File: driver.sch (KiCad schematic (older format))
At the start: 45 parts, among them J1 Screw_Terminal_01x02, J2 Conn_02x12_Odd_Even, Q10 Q_NMOS_GDSD, Q11 Q_NMOS_GDSD, Q12 Q_NMOS_GDSD, Q13 Q_NMOS_GDSD, Q14 Q_NMOS_GDSD, Q15 Q_NMOS_GDSD, Q16 Q_NMOS_GDSD, Q17 AOD417 Q_PMOS_DGS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

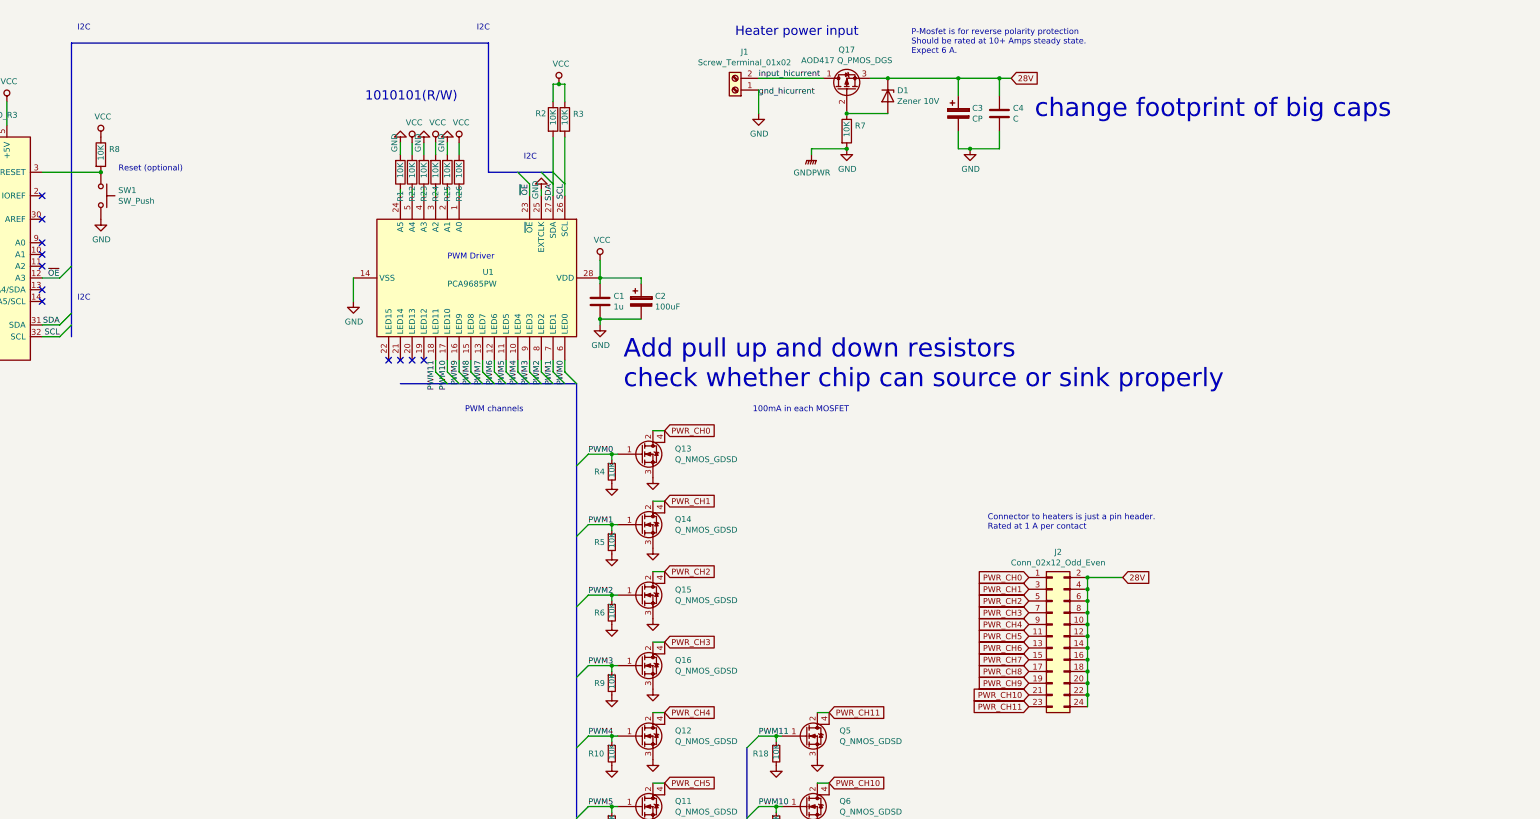
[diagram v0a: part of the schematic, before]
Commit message: remove capacitor footprints and organize.
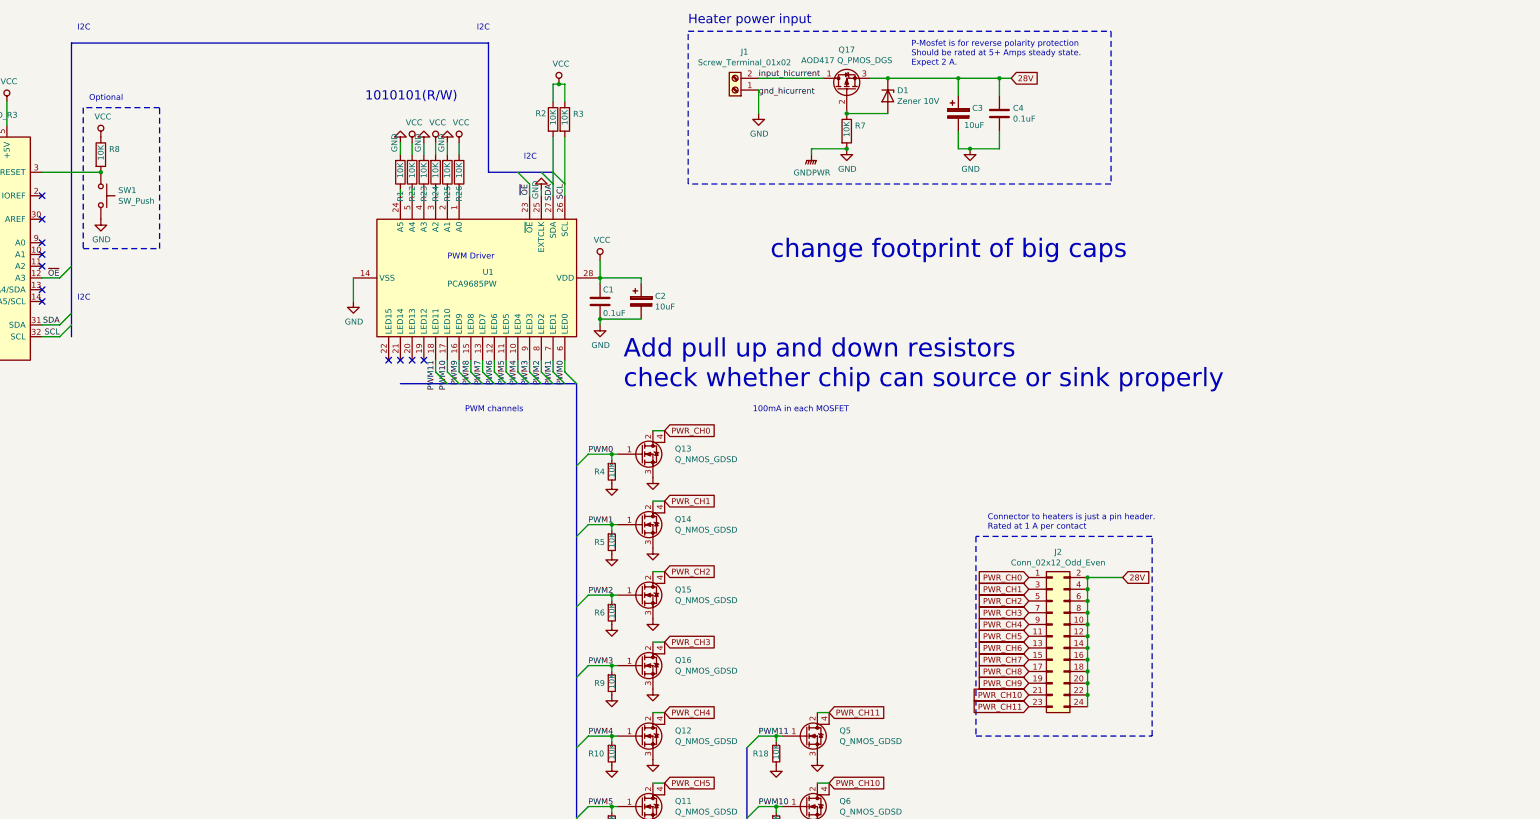
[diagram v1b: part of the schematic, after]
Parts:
- C1: value 1u -> 0.1uF; footprint Capacitor_SMD:C_0805_2012Metric_Pad1.15x1.40mm_HandSolder -> (none)
- C2: value 100uF -> 10uF; footprint Capacitor_THT:CP_Radial_D8.0mm_P3.50mm -> (none)
- C3: value CP -> 10uF
- C4: value C -> 0.1uF
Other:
- note added: "Optional"
- note added: "P-Mosfet is for reverse polarity protection\nShould be rated at 5+ Amps steady state.\nExpect 2 A."
- note removed: "P-Mosfet is for reverse polarity protection\nShould be rated at 10+ Amps steady state.\nExpect 6 A."
- note removed: "Reset (optional)"
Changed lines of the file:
@@
 U 1 1 5C1B80A4
 P 6800 3250
-F 0 "C1" H 6915 3296 50  0000 L CNN
-F 1 "1u" H 6915 3205 50  0000 L CNN
-F 2 "Capacitor_SMD:C_0805_2012Metric_Pad1.15x1.40mm_HandSolder" H 6838 3100 50  0001 C CNN
+F 0 "C1" H 6825 3350 50  0000 L CNN
+F 1 "0.1uF" H 6825 3150 50  0000 L CNN
+F 2 "" H 6838 3100 50  0001 C CNN
 F 3 "~" H 6800 3250 50  0001 C CNN
 	1    6800 3250
@@
 P 7150 3250
 F 0 "C2" H 7268 3296 50  0000 L CNN
-F 1 "100uF" H 7268 3205 50  0000 L CNN
-F 2 "Capacitor_THT:CP_Radial_D8.0mm_P3.50mm" H 7188 3100 50  0001 C CNN
+F 1 "10uF" H 7268 3205 50  0000 L CNN
+F 2 "" H 7188 3100 50  0001 C CNN
 F 3 "~" H 7150 3250 50  0001 C CNN
 	1    7150 3250
@@
 Wire Wire Line
 	8650 6750 8750 6750
-Text Notes 7950 1000 0    79   ~ 0
+Text Notes 7550 900  0    79   ~ 0
 Heater power input
 $Comp
@@
 	1    0    0    -1
 $EndComp
-Text Notes 9450 1150 0    50   ~ 0
-P-Mosfet is for reverse polarity protection\nShould be rated at 10+ Amps steady state.\nExpect 6 A.
+Text Notes 9450 1250 0    50   ~ 0
+P-Mosfet is for reverse polarity protection\nShould be rated at 5+ Amps steady state.\nExpect 2 A.
 Text GLabel 10450 5600 0    50   Input ~ 0
 PWR_CH0
@@
 Text Notes 2350 3250 0    50   ~ 0
 I2C
-Text Notes 2700 2150 0    50   ~ 0
-Reset (optional)
+Text Notes 2450 1550 0    50   ~ 0
+Optional
 Text Notes 5650 4200 0    50   ~ 0
 PWM channels
@@
 P 9850 1650
 F 0 "C3" H 9968 1696 50  0000 L CNN
-F 1 "CP" H 9968 1605 50  0000 L CNN
+F 1 "10uF" H 9900 1550 50  0000 L CNN
 F 2 "" H 9888 1500 50  0001 C CNN
 F 3 "~" H 9850 1650 50  0001 C CNN
@@
 P 10200 1650
 F 0 "C4" H 10315 1696 50  0000 L CNN
-F 1 "C" H 10315 1605 50  0000 L CNN
+F 1 "0.1uF" H 10315 1605 50  0000 L CNN
 F 2 "" H 10238 1500 50  0001 C CNN
 F 3 "~" H 10200 1650 50  0001 C CNN
@@
 Text Notes 7000 4000 0    157  ~ 0
 Add pull up and down resistors\ncheck whether chip can source or sink properly
-Text Notes 10500 1700 0    157  ~ 0
+Text Notes 8250 2900 0    157  ~ 0
 change footprint of big caps
 $Comp
@@
 Wire Wire Line
 	6500 1850 6500 2350
+Wire Notes Line
+	2400 1600 2400 2800
+Wire Notes Line
+	2400 2800 3050 2800
+Wire Notes Line
+	3050 2800 3050 1600
+Wire Notes Line
+	3050 1600 2400 1600
+Wire Notes Line
+	7550 950  11150 950
+Wire Notes Line
+	11150 950  11150 2250
+Wire Notes Line
+	11150 2250 7550 2250
+Wire Notes Line
+	7550 2250 7550 950
+Wire Notes Line
+	10000 5250 10000 6950
+Wire Notes Line
+	10000 6950 11500 6950
+Wire Notes Line
+	11500 6950 11500 5250
+Wire Notes Line
+	11500 5250 10000 5250
+Wire Wire Line
+	6400 1850 6400 2350
 Wire Bus Line
 	5850 2150 6400 2150
-Wire Wire Line
-	6400 1850 6400 2350
 Wire Bus Line
 	8050 7050 8050 9400

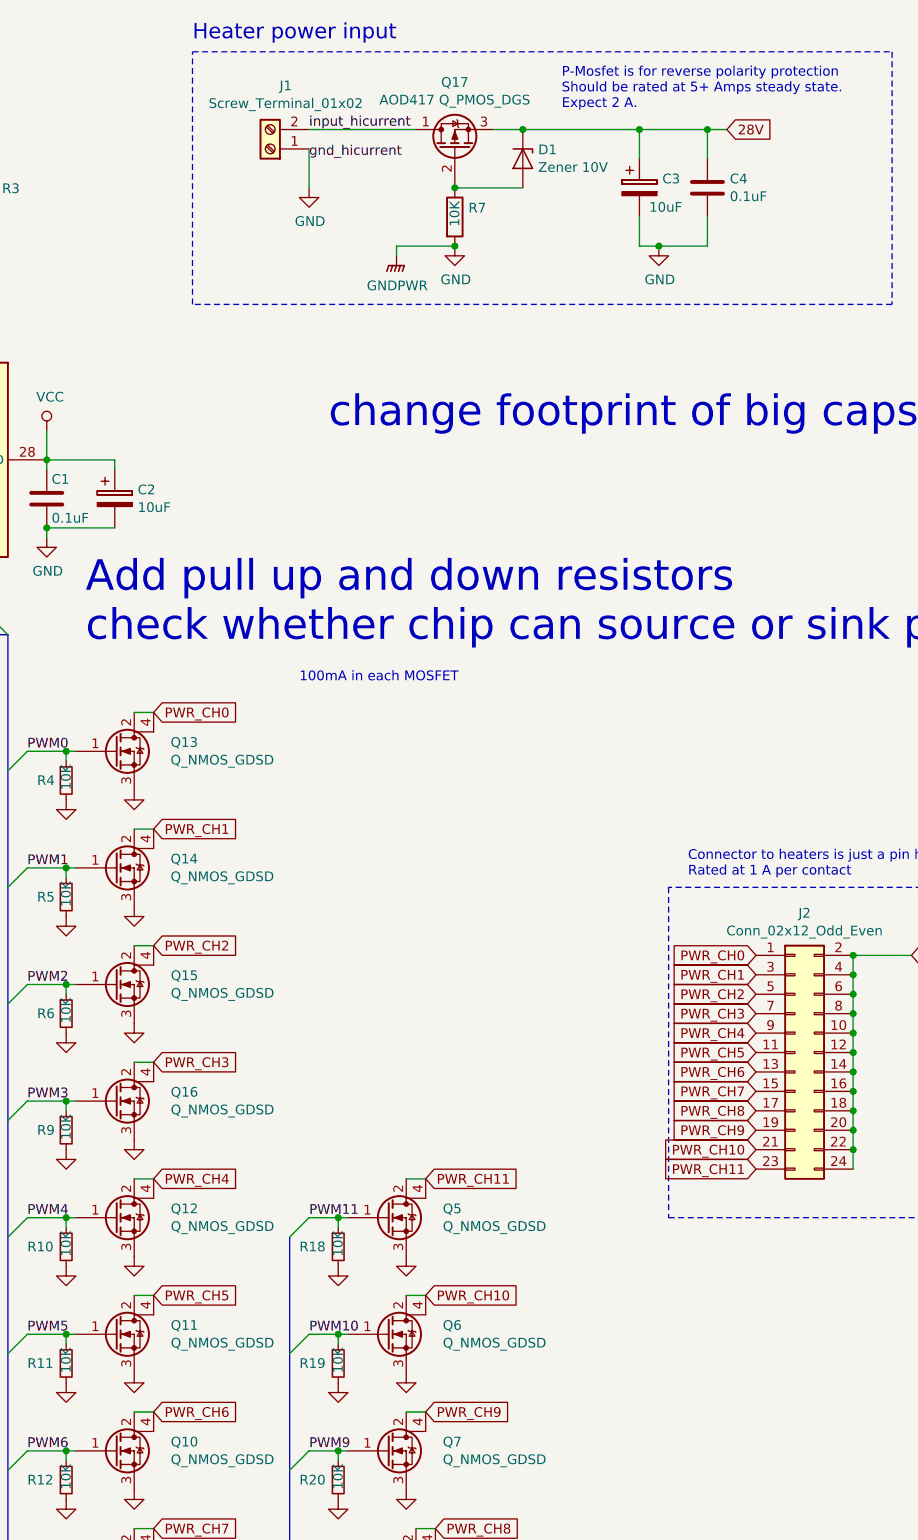
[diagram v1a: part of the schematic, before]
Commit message: replace zener with voltage divdier, swap MOSFETs, update footprints, separate power and signal ground planes
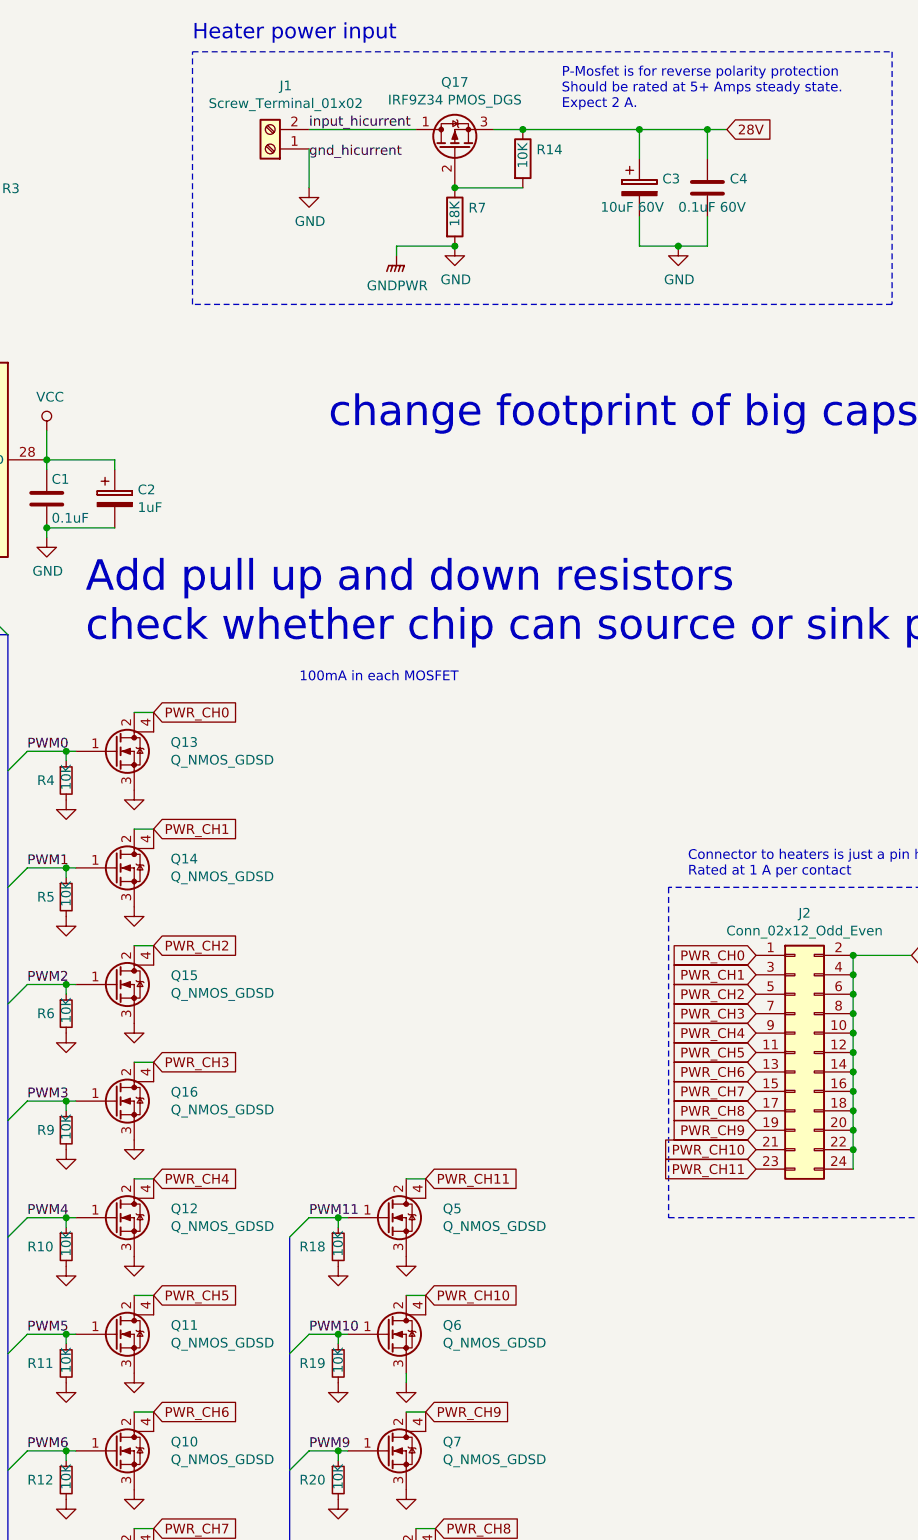
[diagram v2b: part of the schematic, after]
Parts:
- removed D1: Zener 10V, Diode_SMD:D_1206_3216Metric_Pad1.42x1.75mm_HandSolder, symbol Device:D_Zener
- added R14: 10K, Resistor_SMD:R_0805_2012Metric_Pad1.15x1.40mm_HandSolder, symbol Device:R
- C1: footprint (none) -> Capacitor_SMD:C_1210_3225Metric_Pad1.42x2.65mm_HandSolder
- C2: value 10uF -> 1uF
- C3: value 10uF -> 10uF 60V
- C4: value 0.1uF -> 0.1uF 60V; footprint (none) -> Capacitor_SMD:C_1210_3225Metric_Pad1.42x2.65mm_HandSolder
- Q17: value AOD417 Q_PMOS_DGS -> IRF9Z34 PMOS_DGS; footprint Package_TO_SOT_SMD:TO-252-2 -> Package_TO_SOT_THT:TO-220-3_Vertical
- R7: value 10K -> 18K
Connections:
- net 28V: now also R14.1
- net at Q17.2 (G), R7.1: now also R14.2
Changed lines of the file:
@@
 F 0 "C1" H 6825 3350 50  0000 L CNN
 F 1 "0.1uF" H 6825 3150 50  0000 L CNN
-F 2 "" H 6838 3100 50  0001 C CNN
+F 2 "Capacitor_SMD:C_1210_3225Metric_Pad1.42x2.65mm_HandSolder" H 6838 3100 50  0001 C CNN
 F 3 "~" H 6800 3250 50  0001 C CNN
 	1    6800 3250
@@
 P 7150 3250
 F 0 "C2" H 7268 3296 50  0000 L CNN
-F 1 "10uF" H 7268 3205 50  0000 L CNN
+F 1 "1uF" H 7268 3205 50  0000 L CNN
 F 2 "" H 7188 3100 50  0001 C CNN
 F 3 "~" H 7150 3250 50  0001 C CNN
@@
 L power:GND #PWR06
 U 1 1 5C4236C9
-P 8650 7750
-F 0 "#PWR06" H 8650 7500 50  0001 C CNN
-F 1 "GND" H 8655 7577 50  0001 C CNN
-F 2 "" H 8650 7750 50  0001 C CNN
-F 3 "" H 8650 7750 50  0001 C CNN
-	1    8650 7750
+P 8650 7800
+F 0 "#PWR06" H 8650 7550 50  0001 C CNN
+F 1 "GND" H 8655 7627 50  0001 C CNN
+F 2 "" H 8650 7800 50  0001 C CNN
+F 3 "" H 8650 7800 50  0001 C CNN
+	1    8650 7800
 	-1   0    0    -1
 $EndComp
@@
 P 8900 1450
 F 0 "Q17" V 9243 1450 50  0000 C CNN
-F 1 "AOD417 Q_PMOS_DGS" V 9152 1450 50  0000 C CNN
-F 2 "Package_TO_SOT_SMD:TO-252-2" H 9100 1550 50  0001 C CNN
+F 1 "IRF9Z34 PMOS_DGS" V 9152 1450 50  0000 C CNN
+F 2 "Package_TO_SOT_THT:TO-220-3_Vertical" H 9100 1550 50  0001 C CNN
 F 3 "~" H 8900 1450 50  0001 C CNN
 	1    8900 1450
@@
 Wire Wire Line
 	8150 1350 8700 1350
-$Comp
-L Device:D_Zener D1
-U 1 1 5C42C2C0
-P 9250 1500
-F 0 "D1" V 9204 1579 50  0000 L CNN
-F 1 "Zener 10V" V 9295 1579 50  0000 L CNN
-F 2 "Diode_SMD:D_1206_3216Metric_Pad1.42x1.75mm_HandSolder" H 9250 1500 50  0001 C CNN
-F 3 "~" H 9250 1500 50  0001 C CNN
-	1    9250 1500
-	0    1    1    0
-$EndComp
-Wire Wire Line
-	9100 1350 9250 1350
 $Comp
 L power:GND #PWR019
@@
 P 8900 1800
 F 0 "R7" H 8970 1846 50  0000 L CNN
-F 1 "10K" V 8900 1750 50  0000 L CNN
+F 1 "18K" V 8900 1750 50  0000 L CNN
 F 2 "Resistor_SMD:R_0805_2012Metric_Pad1.15x1.40mm_HandSolder" V 8830 1800 50  0001 C CNN
 F 3 "~" H 8900 1800 50  0001 C CNN
@@
 Text GLabel 10300 1350 2    50   Input ~ 0
 28V
-Connection ~ 9250 1350
 Text Label 8150 1350 0    50   ~ 0
 input_hicurrent
@@
 L power:GND #PWR021
 U 1 1 5C43FABC
-P 9950 1950
-F 0 "#PWR021" H 9950 1700 50  0001 C CNN
-F 1 "GND" H 9955 1777 50  0000 C CNN
-F 2 "" H 9950 1950 50  0001 C CNN
-F 3 "" H 9950 1950 50  0001 C CNN
-	1    9950 1950
+P 10050 1950
+F 0 "#PWR021" H 10050 1700 50  0001 C CNN
+F 1 "GND" H 10055 1777 50  0000 C CNN
+F 2 "" H 10050 1950 50  0001 C CNN
+F 3 "" H 10050 1950 50  0001 C CNN
+	1    10050 1950
 	1    0    0    -1
 $EndComp
@@
 Text Notes 11900 10300 0    157  ~ 0
 Heater Driver PCB
-Wire Wire Line
-	9250 1350 9850 1350
 $Comp
 L Device:CP C3
@@
 P 9850 1650
 F 0 "C3" H 9968 1696 50  0000 L CNN
-F 1 "10uF" H 9900 1550 50  0000 L CNN
+F 1 "10uF 60V" H 9650 1550 50  0000 L CNN
 F 2 "" H 9888 1500 50  0001 C CNN
 F 3 "~" H 9850 1650 50  0001 C CNN
@@
 P 10200 1650
 F 0 "C4" H 10315 1696 50  0000 L CNN
-F 1 "0.1uF" H 10315 1605 50  0000 L CNN
-F 2 "" H 10238 1500 50  0001 C CNN
+F 1 "0.1uF 60V" H 10050 1550 50  0000 L CNN
+F 2 "Capacitor_SMD:C_1210_3225Metric_Pad1.42x2.65mm_HandSolder" H 10238 1500 50  0001 C CNN
 F 3 "~" H 10200 1650 50  0001 C CNN
 	1    10200 1650
@@
 	9850 1800 9850 1950
 Wire Wire Line
-	9850 1950 9950 1950
-Wire Wire Line
-	9950 1950 10200 1950
+	10050 1950 10200 1950
 Wire Wire Line
 	10200 1950 10200 1800
-Connection ~ 9950 1950
 $Comp
 L Device:R R3
@@
 NoConn ~ 5000 3750
 NoConn ~ 5300 3750
-Wire Wire Line
-	6500 1850 6500 2350
 Wire Notes Line
 	2400 1600 2400 2800
@@
 	11500 5250 10000 5250
 Wire Wire Line
+	6500 1850 6500 2350
+Wire Wire Line
+	9100 1350 9250 1350
+$Comp
+L Device:R R14
+U 1 1 5C4FCB04
+P 9250 1500
+F 0 "R14" H 9320 1546 50  0000 L CNN
+F 1 "10K" V 9250 1450 50  0000 L CNN
+F 2 "Resistor_SMD:R_0805_2012Metric_Pad1.15x1.40mm_HandSolder" V 9180 1500 50  0001 C CNN
+F 3 "~" H 9250 1500 50  0001 C CNN
+	1    9250 1500
+	1    0    0    -1
+$EndComp
+Connection ~ 9250 1350
+Wire Wire Line
+	9250 1350 9850 1350
+Wire Wire Line
+	8650 7750 8650 7800
+Connection ~ 10050 1950
+Wire Wire Line
+	9850 1950 10050 1950
+Wire Wire Line
 	6400 1850 6400 2350
